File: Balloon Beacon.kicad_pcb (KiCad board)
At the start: 2 copper layers, 46 parts, among them J1 PV Input, J2 Serial, J3 ICSP, J4 I2C, J6 GPS_ANT, Q1 AO3401A, Q2 AO3401A, U1 XC6206P332MR, U2 ATmega328PB-MU, U3 STC22K33048-26.000MT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

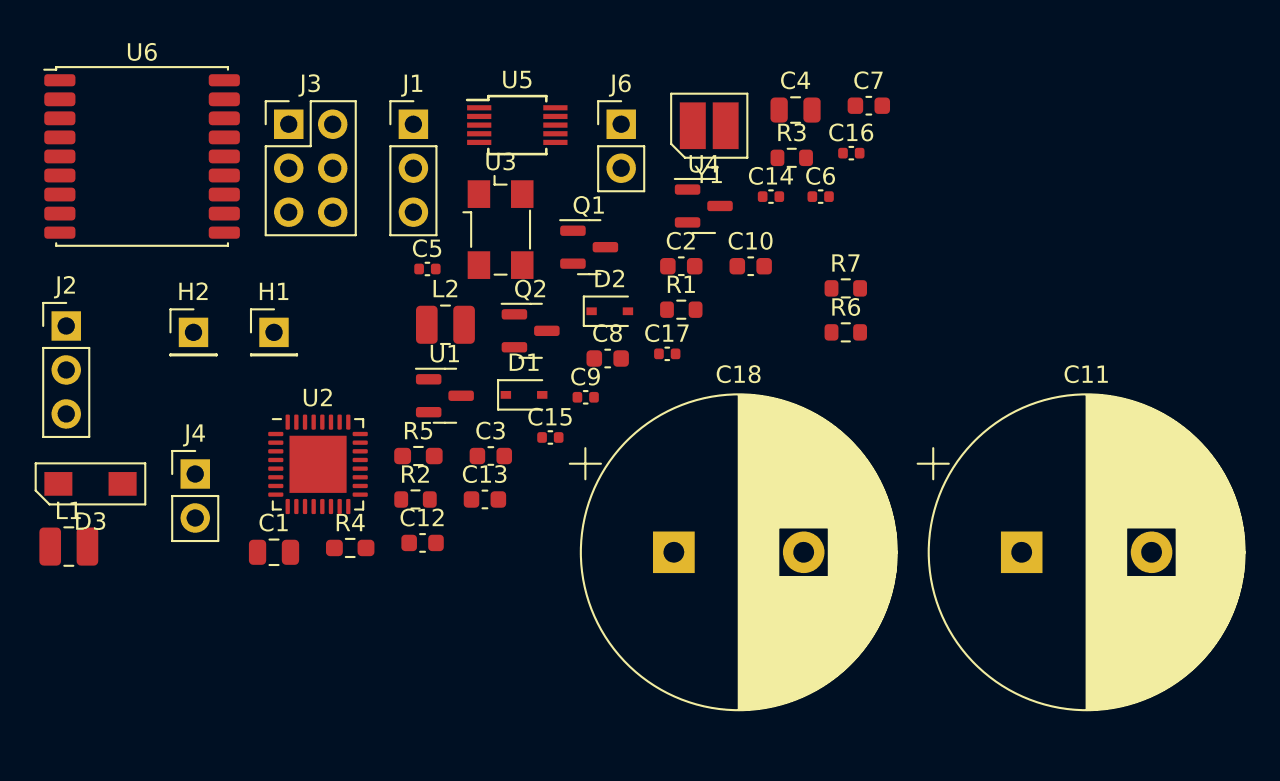
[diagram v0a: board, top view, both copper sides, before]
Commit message: Changed TCXO to an available one.
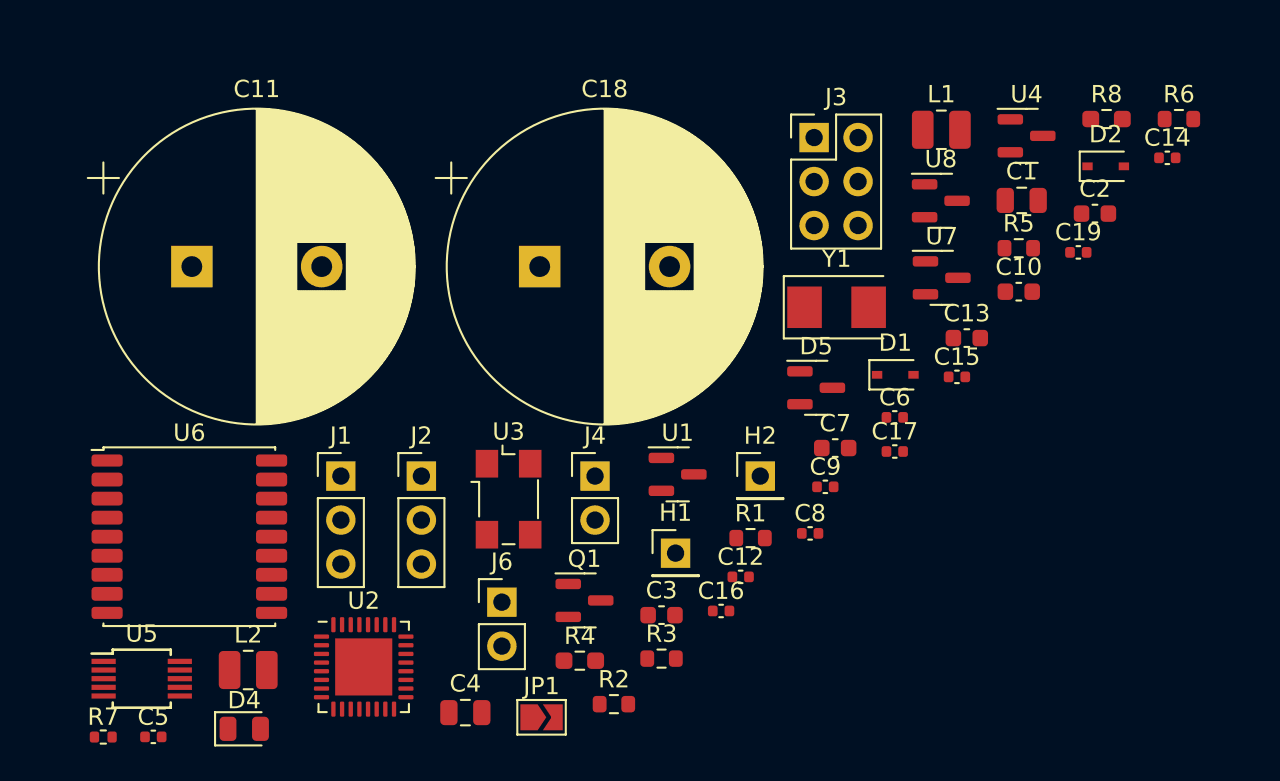
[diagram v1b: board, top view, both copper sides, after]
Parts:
- removed D3: ZMM5V6, Balloon:ll-34
- removed Q2: AO3401A, Package_TO_SOT_SMD:SOT-23
- added C19: 0.1uF, Capacitor_SMD:C_0402_1005Metric, F.Cu at (82.0, 25.9)
- added D4: Status, LED_SMD:LED_0805_2012Metric, F.Cu at (33.8, 53.4)
- added D5: CM1214A, Package_TO_SOT_SMD:SOT-23, F.Cu at (66.9, 33.7)
- added JP1: SolderJumper_2_Open, Jumper:SolderJumper-2_P1.3mm_Open_TrianglePad1.0x1.5mm, F.Cu at (51.0, 52.7)
- added R8: 100, Resistor_SMD:R_0603_1608Metric_Pad0.98x0.95mm_HandSolder, F.Cu at (83.6, 18.2)
- added U7: CJ431, Package_TO_SOT_SMD:SOT-23, F.Cu at (74.1, 27.3)
- added U8: CJ431, Package_TO_SOT_SMD:SOT-23, F.Cu at (74.1, 22.9)
- C10, C7: value 8 pF -> 10 pF
- C12: value 10nF -> 0.1uF; footprint Capacitor_SMD:C_0603_1608Metric -> Capacitor_SMD:C_0402_1005Metric
- C13: value 0.47uF -> 22 uF
- C3: value 1 uF -> 22 uF
- C8: value 1 uF -> 0.1uF; footprint Capacitor_SMD:C_0603_1608Metric -> Capacitor_SMD:C_0402_1005Metric
- R1: value 10k -> 16k
- R5: value 1.5k -> 16k; footprint Resistor_SMD:R_0603_1608Metric_Pad0.98x0.95mm_HandSolder -> Resistor_SMD:R_0603_1608Metric
- R6: value 10k -> 43k
- R7: value 10k -> 100k; footprint Resistor_SMD:R_0603_1608Metric -> Resistor_SMD:R_0402_1005Metric
- U1: value XC6206P332MR -> CJ431
- Y1: value 16 MHz -> 8 MHz; footprint Balloon:NDK xtal -> Crystal:Crystal_SMD_5032-2Pin_5.0x3.2mm
- moved L1 55.8 mm to (74.1, 18.8)
- moved C11 50.7 mm to (30.8, 26.7)
- moved R7 50.1 mm to (25.7, 53.9)
- moved C1 47.7 mm to (78.7, 22.9)
- moved C4 39.7 mm to (46.6, 52.4)
- moved U5 38.6 mm to (27.9, 50.5)
- moved R5 36.7 mm to (78.6, 25.6)
- moved H2 33.8 mm to (63.6, 38.8)
- moved C5 31.3 mm to (28.6, 53.8)
- moved J3 30.3 mm to (66.8, 19.2)
- moved R3 29.9 mm to (57.9, 49.3)
- moved D2 29.8 mm to (83.6, 20.9)
- moved C13 29.3 mm to (75.6, 30.8)
- moved J6 28.4 mm to (48.7, 46.1)
- moved C16 27.5 mm to (61.4, 46.6)
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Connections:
- C11 pad 1: /VDD -> +3V3
- C13 pad 1: Net-(C13-Pad1) -> +3V3
- C16 pad 1: /VDD -> +3V3
- C3 pad 1: /VDD -> +3V3
- C5 pad 2: +3V3 -> /RESET
- D1 pad 1: /VDD -> +3V3
- D2 pad 1: /VDD -> +3V3
- R5 pad 1: /GPS_E -> Net-(C4-Pad2)
- R5 pad 2: Net-(Q2-Pad1) -> GND
- R6 pad 1: /VDD -> +3V3
- U1 pad 1: GND -> +3V3
- U1 pad 2: +3V3 -> /VDD_TST
- U1 pad 3: /VDD -> GND
- U2 pad 22: unconnected-(U2-Pad22) -> Net-(D4-Pad2)
- U2 pad 3: GND -> unconnected-(U2-Pad3)
- U2 pad 6: +3V3 -> unconnected-(U2-Pad6)
- U3 pad 3: Net-(C12-Pad1) -> Net-(C12-Pad2)
- U4 pad 1: /VDD -> +3V3
- U5 pad 2: Net-(C12-Pad2) -> Net-(C12-Pad1)
- U6 pad 7: unconnected-(U6-Pad7) -> Net-(JP1-Pad1)
- U6 pad 8: Net-(C13-Pad1) -> +3V3
- U6 pad 9: Net-(C13-Pad1) -> +3V3
